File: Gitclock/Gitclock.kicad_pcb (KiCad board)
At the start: 2 copper layers, 140 x 90 mm, 49 parts, among them J1 PJ-102AH, J2 Conn_01x06, J3 Conn_02x03_Odd_Even, Q1 NPN_2N3904_SOT23, SW1 Omron_B3F_SPST, SW5 RotaryEncoder_Switch, U1 ATmega328-PU, U2 L7805, U3 MAX7219, U4 DS1307_DIP-8, Y1 Crystal_16MHz, Y2 Crystal_32768Hz

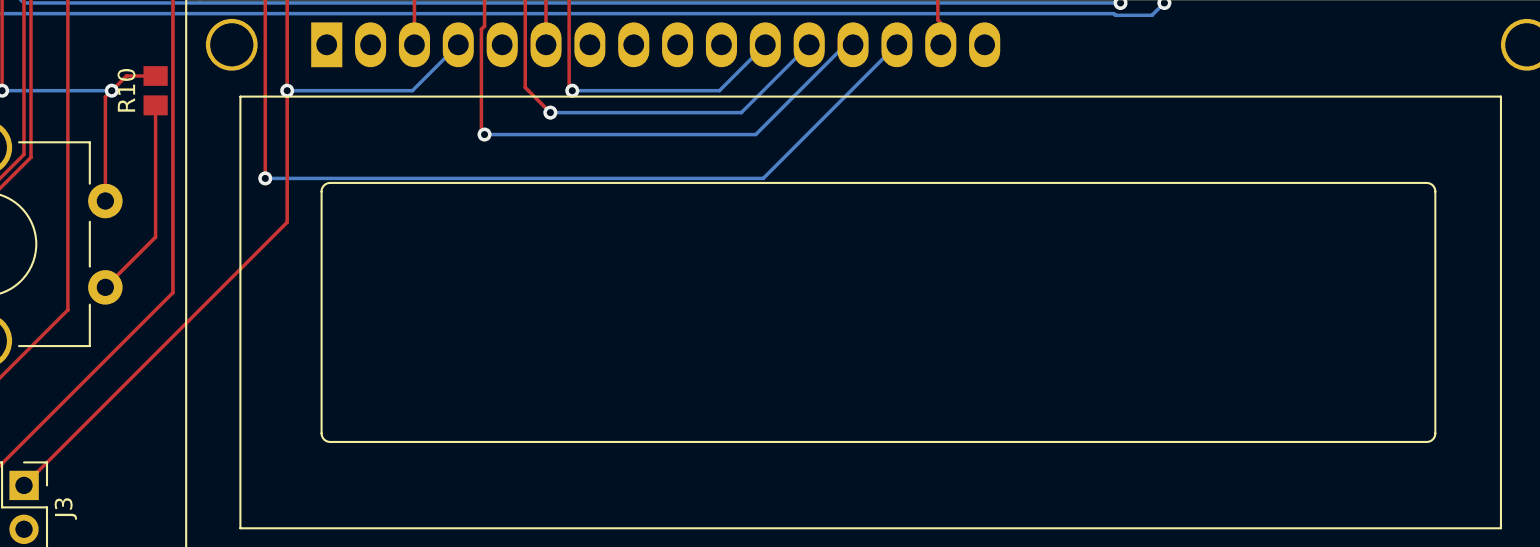
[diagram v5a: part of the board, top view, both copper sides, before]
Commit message: Changed Encoder connection on SW from VCC to GND
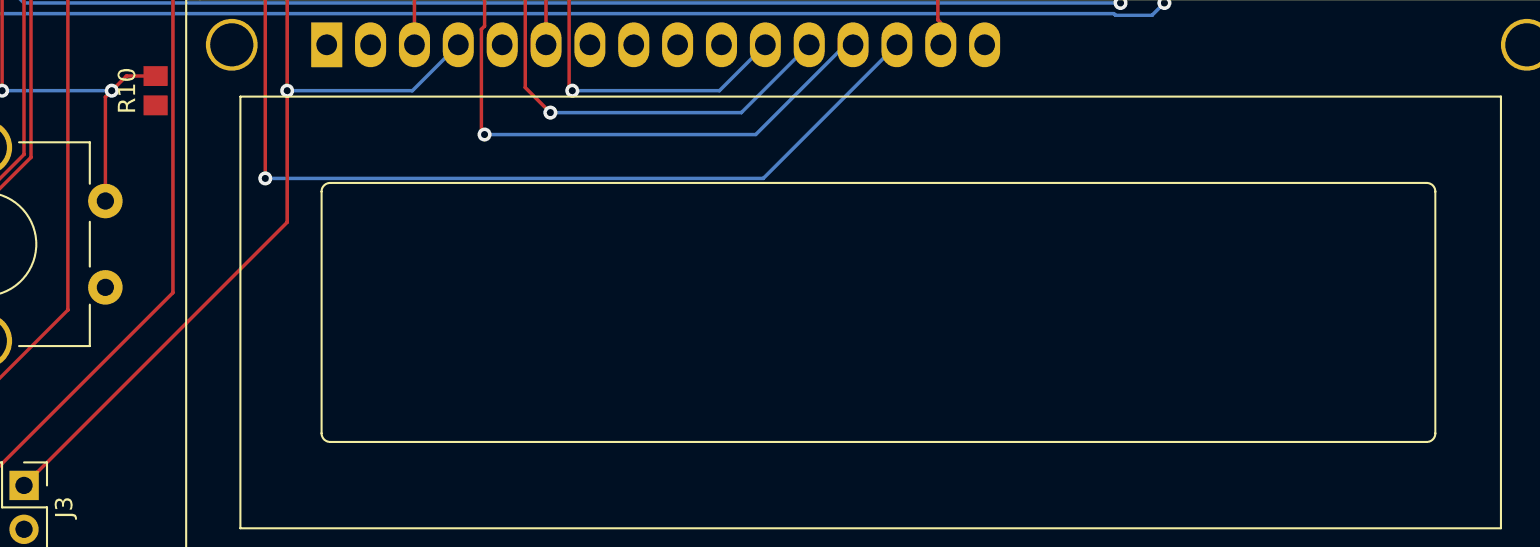
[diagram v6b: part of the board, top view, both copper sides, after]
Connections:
- SW5 pad S1: VCC -> GND
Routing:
- net VCC: track 11.7 -> 0.00 mm
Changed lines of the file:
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@@
     (fp_line (start 63.70066 23) (end 0.2 23) (layer "F.SilkS") (width 0.12))
     (fp_arc (start 0.20066 22.9997) (mid -0.153162 22.853142) (end -0.29972 22.49932) (layer "F.SilkS") (width 0.12))
-    (fp_arc (start 64.20104 22.49932) (mid 64.054473 22.853115) (end 63.70066 22.9997) (layer "F.SilkS") (width 0.12))
+    (fp_arc (start 64.20104 22.49932) (mid 64.054479 22.85315) (end 63.70066 22.9997) (layer "F.SilkS") (width 0.12))
     (fp_arc (start -0.29972 8.49884) (mid -0.153162 8.145018) (end 0.20066 7.99846) (layer "F.SilkS") (width 0.12))
     (fp_arc (start 63.7 8) (mid 64.053553 8.146447) (end 64.2 8.5) (layer "F.SilkS") (width 0.12))
@@
       (net 1 "GND") (pinfunction "C") (pintype "passive"))
     (pad "S1" thru_hole circle (at 14.5 5) (size 2 2) (drill 1) (layers *.Cu *.Mask)
-      (net 34 "VCC") (pinfunction "S1") (pintype "passive"))
+      (net 1 "GND") (pinfunction "S1") (pintype "passive"))
     (pad "S2" thru_hole circle (at 14.5 0) (size 2 2) (drill 1) (layers *.Cu *.Mask)
       (net 36 "MENU_B") (pinfunction "S2") (pintype "passive"))
@@
   (segment (start 151.98 103.8525) (end 152.15 104.0225) (width 0.2032) (layer "F.Cu") (net 29))
   (segment (start 151.98 99.06) (end 151.98 103.8525) (width 0.2032) (layer "F.Cu") (net 29))
-  (segment (start 106.68 116.43) (end 106.68 108.8) (width 0.2032) (layer "F.Cu") (net 34))
-  (segment (start 103.77 119.34) (end 106.68 116.43) (width 0.2032) (layer "F.Cu") (net 34))
   (segment (start 99.06 78.74) (end 101.59 76.21) (width 0.2032) (layer "F.Cu") (net 35))
   (segment (start 86.36 115.15) (end 87.17 114.34) (width 0.2032) (layer "F.Cu") (net 35))
